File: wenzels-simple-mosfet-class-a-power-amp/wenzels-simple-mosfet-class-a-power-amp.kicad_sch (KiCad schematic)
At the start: 30 parts, among them J1 48V, J2 INPUT, J3 SPEAKER, Q1 IRFP240, SW1 POWER ON

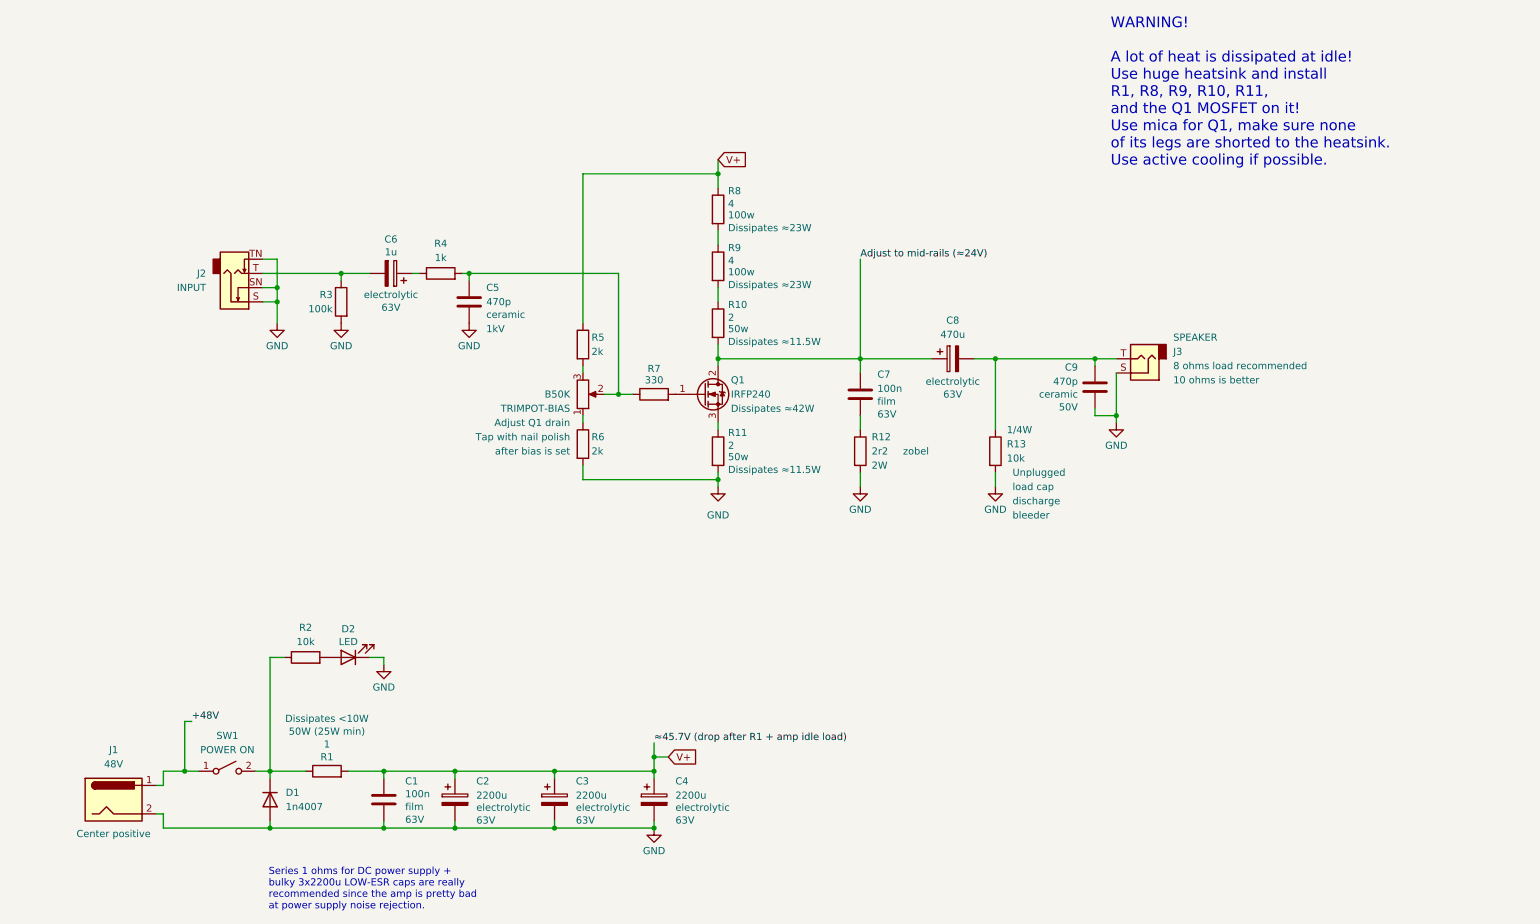
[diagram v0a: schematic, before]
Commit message: wenzels-simple-mosfet-class-a-power-amp r1-wip-2
Add a K170 JFET gain stage in front of the MOSFET.
It both adds gain and inverts the phase back to match the input
(K170 inverting + MOSFET inverting = restored phase polarity).
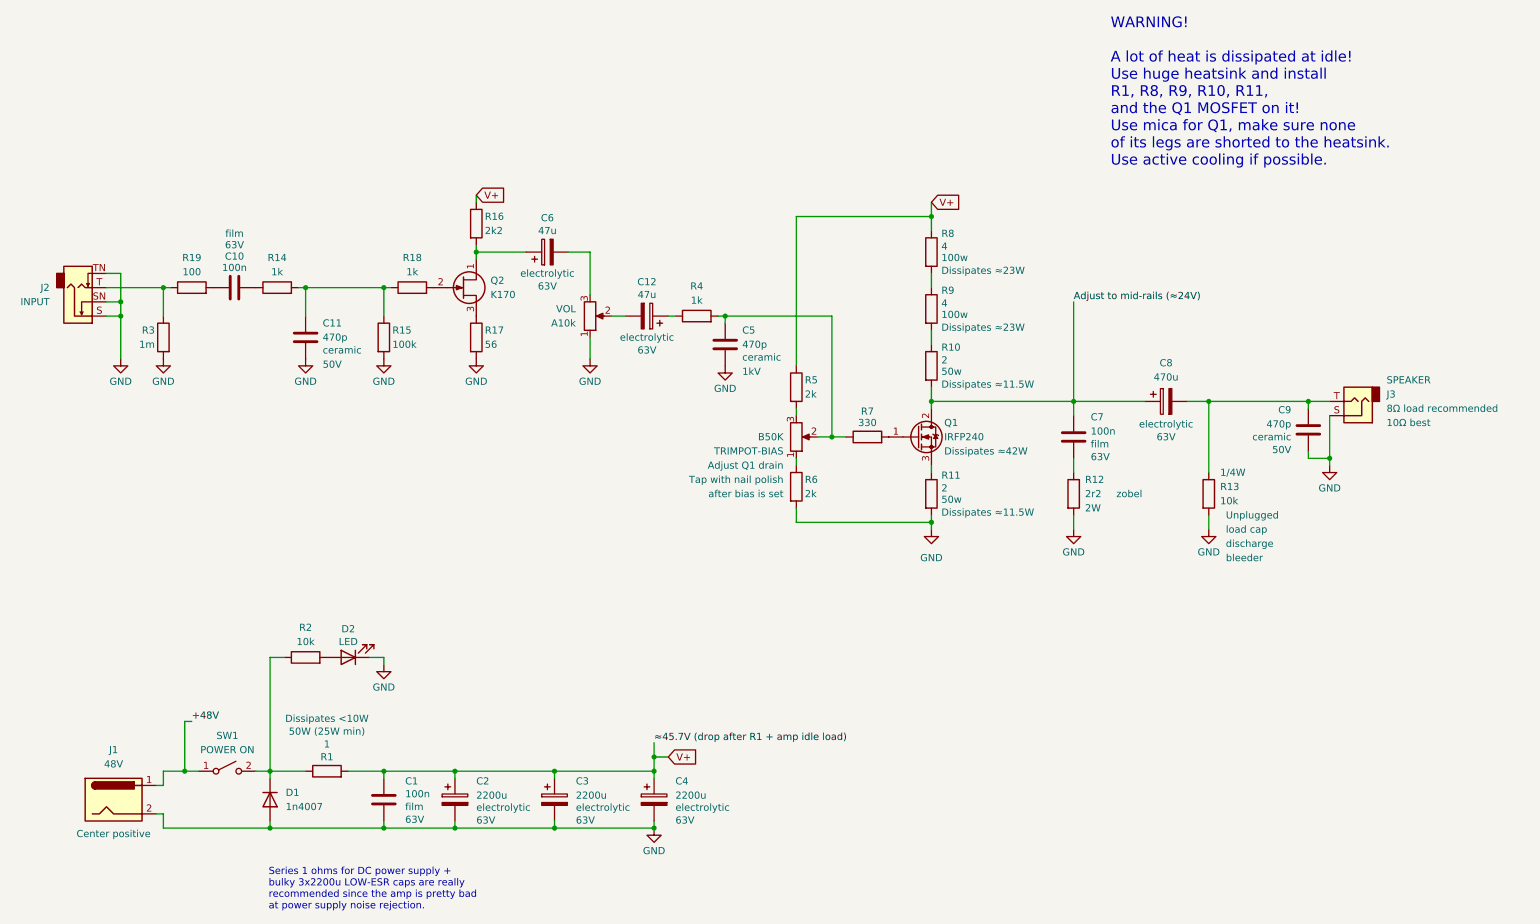
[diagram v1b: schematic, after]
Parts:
- added C10: 100n, symbol Device:C
- added C11: 470p, symbol Device:C
- added C12: 47u, symbol Device:C_Polarized
- added Q2: K170, Package_TO_SOT_THT:TO-92, symbol Transistor_FET:2N3819
- added R14, R18: 1k, symbol Device:R
- added R15: 100k, symbol Device:R
- added R16: 2k2, symbol Device:R
- added R17: 56, symbol Device:R
- added R19: 100, symbol Device:R
- added VOL: A10k, symbol Device:R_Potentiometer
- C6: value 1u -> 47u
- J3: Field5 8 ohms load recommended -> 8Ω load recommended; Field6 10 ohms is better -> 10Ω best
- R3: value 100k -> 1m
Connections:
- net GND: now also C11.2, R15.2, R17.2, VOL.1
- net V+: now also R16.1
- net at J2.T, R3.1: now also R19.1; no longer C6.2
- net at R4.1: now also C12.1; no longer C6.1
- new net: C10.2, R14.1
- new net: C11.1, R14.2, R15.1, R18.1
- new net: C12.2, VOL.2
- new net: Q2.3 (S), R17.1
- new net: C10.1, R19.2
- new net: C6.1, Q2.1 (D), R16.2
- new net: C6.2, VOL.3
- new net: Q2.2 (G), R18.2
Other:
- moved on the sheet: C5, C6, C7, C8, C9, J2, J3, Q1, R10, R11, R12, R13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
